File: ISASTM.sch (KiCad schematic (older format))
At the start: 137 parts, among them J1 Bus_ISA_8bit, J2 USB_C_Receptacle_USB2.0, J3 Boot select, J4 USB_C_Receptacle_USB2.0, J5 TagConnect_TC2030_SWD, SW1 Reset, U1 STM32H743IITx, U10 SN74AVC8T245PW, U11 SN74AVC8T245PW, U12 SN74AVC8T245PW, U13 SN74AVC8T245PW, U14 SRV05-4, U15 USB3343, U2 MT48LC16M16A2P, U3 SN74AVC8T245PW, U4 SN74AVC8T245PW, U5 AMS1117-3.3, U6 SN74AVC8T245PW, U7 SN74AVC8T245PW, U8 SN74AVC8T245PW, U9 SN74AVC8T245PW, X1 SG-7050CAN, Y1 26 MHz, Y2 8 MHz

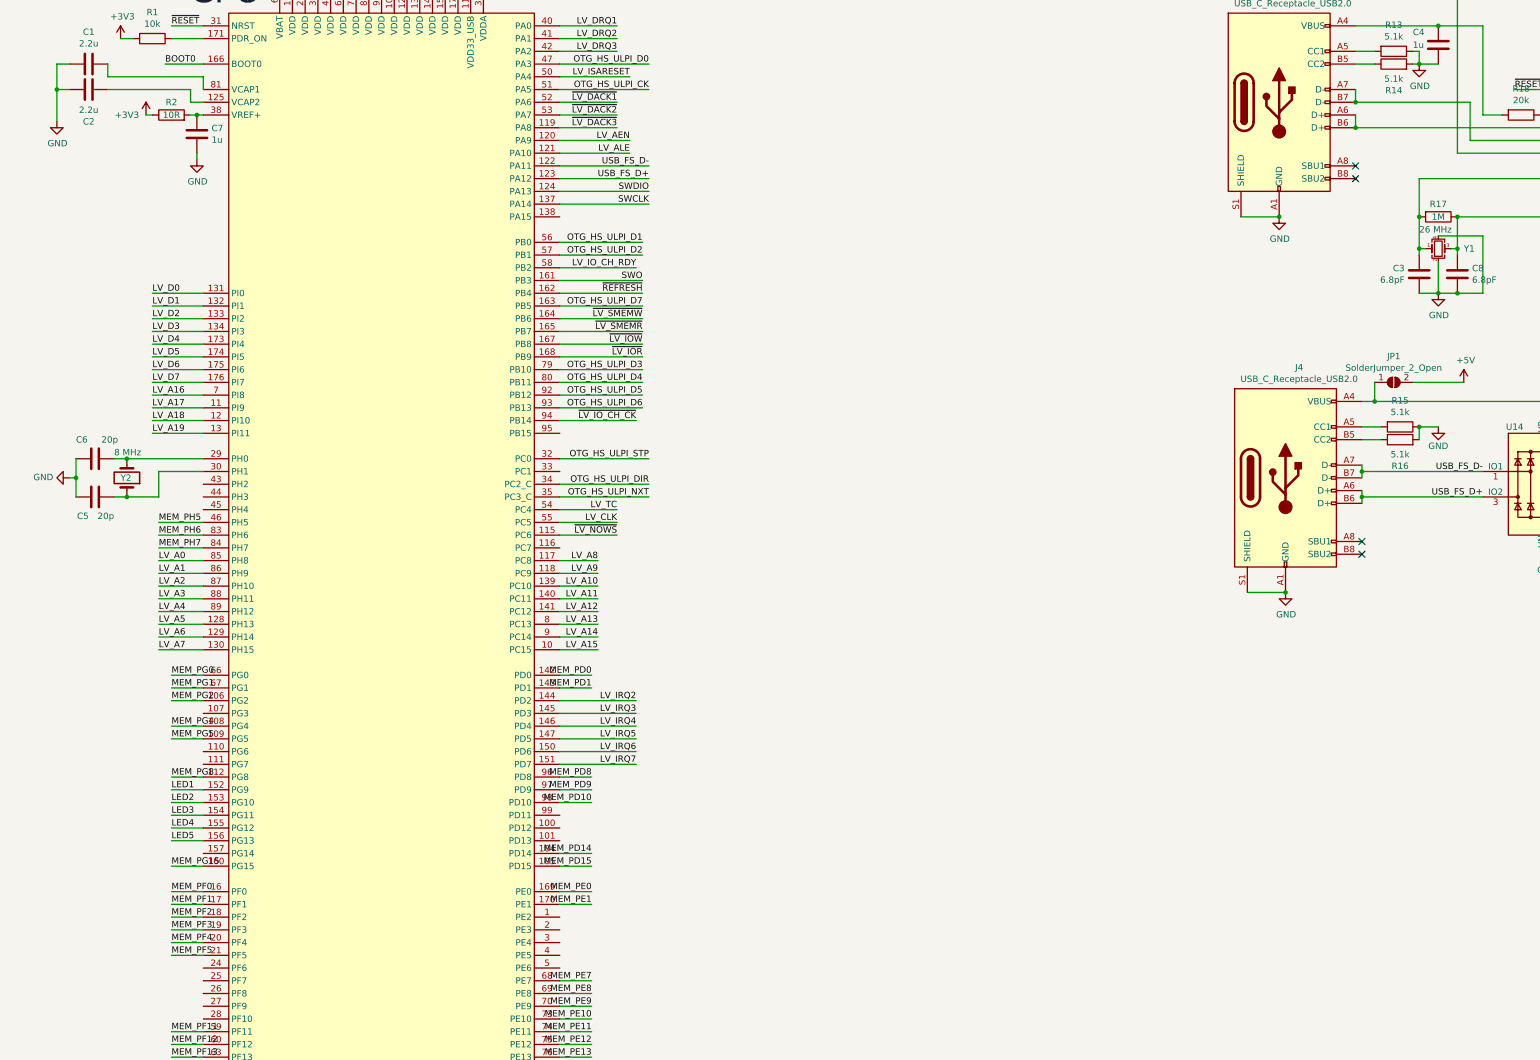
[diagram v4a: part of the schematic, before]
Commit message: Finish fanout and ULPI routing
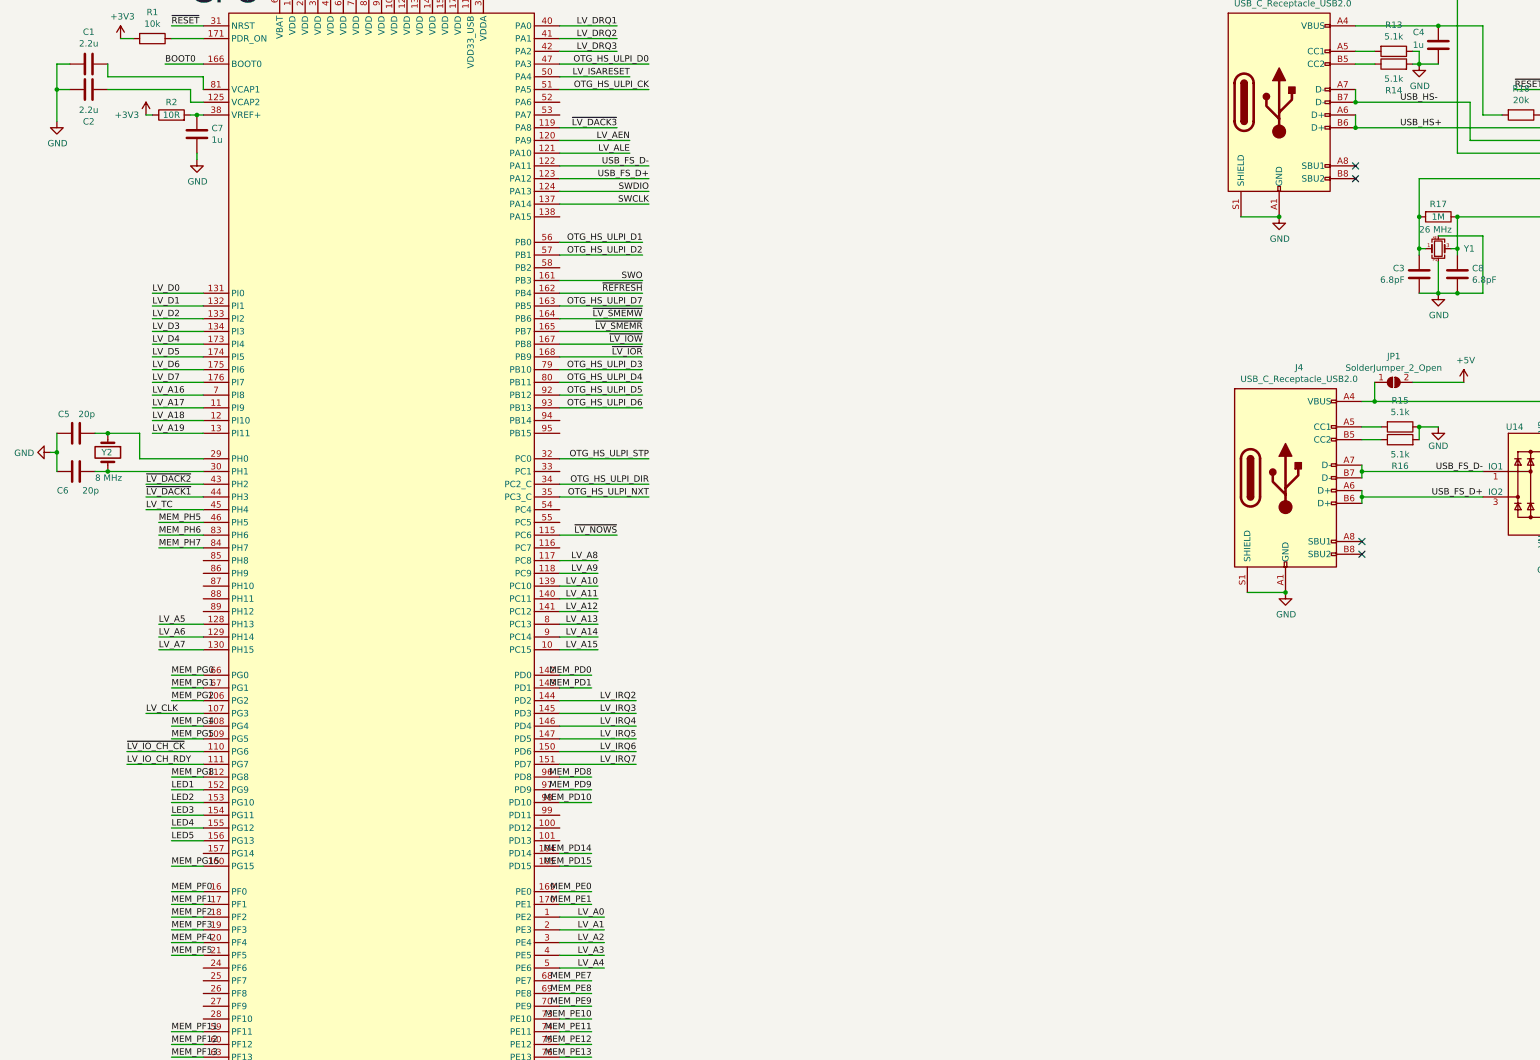
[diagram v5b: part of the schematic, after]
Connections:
- net LV_A0: now also U1.1 (PE2); no longer U1.85 (PH8)
- net LV_A1: now also U1.2 (PE3); no longer U1.86 (PH9)
- net LV_A2: now also U1.3 (PE4); no longer U1.87 (PH10)
- net LV_A3: now also U1.4 (PE5); no longer U1.88 (PH11)
- net LV_A4: now also U1.5 (PE6); no longer U1.89 (PH12)
- net LV_CLK: now also U1.107 (PG3); no longer U1.55 (PC5)
- net LV_IO_CH_RDY: now also U1.111 (PG7); no longer U1.58 (PB2)
- net LV_TC: now also U1.45 (PH4); no longer U1.54 (PC4)
- net ~LV_DACK1: now also U1.44 (PH3); no longer U1.52 (PA6)
- net ~LV_DACK2: now also U1.43 (PH2); no longer U1.53 (PA7)
- net ~LV_IO_CH_CK: now also U1.110 (PG6); no longer U1.94 (PB14)
- net at C6.1, Y2.2: now also U1.30 (PH1); no longer U1.29 (PH0)
- net at C5.2, Y2.1: now also U1.29 (PH0); no longer U1.30 (PH1)
- net USB_HS+: now reaches J2.A6 (D+), J2.B6 (D+), U15.13 (DP)
- net USB_HS-: now reaches J2.A7 (D-), J2.B7 (D-), U15.14 (DM)
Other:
- moved on the sheet: C5, C6, Y2
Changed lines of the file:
@@
 L Device:Crystal Y?
 U 1 1 5FB0B2CB
-P 1450 4750
+P 1300 4550
 AR Path="/5F65970E/5FB0B2CB" Ref="Y?"  Part="1"
 AR Path="/5FB0B2CB" Ref="Y2"  Part="1"
-F 0 "Y2" V 1450 4700 50  0000 L CNN
-F 1 "8 MHz" V 1650 4650 50  0000 L CNN
-F 2 "Crystal:Crystal_SMD_5032-2Pin_5.0x3.2mm" H 1450 4750 50  0001 C CNN
-F 3 "~" H 1450 4750 50  0001 C CNN
-F 4 "C115962" V 1450 4750 50  0001 C CNN "LCSC"
-	1    1450 4750
-	0    1    -1   0
+F 0 "Y2" V 1300 4500 50  0000 L CNN
+F 1 "8 MHz" V 1500 4450 50  0000 L CNN
+F 2 "Crystal:Crystal_SMD_5032-2Pin_5.0x3.2mm" H 1300 4550 50  0001 C CNN
+F 3 "~" H 1300 4550 50  0001 C CNN
+F 4 "C115962" V 1300 4550 50  0001 C CNN "LCSC"
+	1    1300 4550
+	0    1    1    0
 $EndComp
 $Comp
 L Device:C C?
 U 1 1 5FB0B2F2
-P 1200 4900
+P 1050 4400
 AR Path="/5F65970E/5FB0B2F2" Ref="C?"  Part="1"
 AR Path="/5FB0B2F2" Ref="C5"  Part="1"
-F 0 "C5" V 1350 4950 50  0000 L CNN
-F 1 "20p" V 1350 4750 50  0000 L CNN
-F 2 "Capacitor_SMD:C_0402_1005Metric" H 1238 4750 50  0001 C CNN
-F 3 "~" H 1200 4900 50  0001 C CNN
-F 4 "C1554" H 1200 4900 50  0001 C CNN "LCSC"
-	1    1200 4900
-	0    -1   1    0
+F 0 "C5" V 1200 4450 50  0000 L CNN
+F 1 "20p" V 1200 4250 50  0000 L CNN
+F 2 "Capacitor_SMD:C_0402_1005Metric" H 1088 4250 50  0001 C CNN
+F 3 "~" H 1050 4400 50  0001 C CNN
+F 4 "C1554" H 1050 4400 50  0001 C CNN "LCSC"
+	1    1050 4400
+	0    -1   -1   0
 $EndComp
 $Comp
 L Device:C C?
 U 1 1 5FB0B2F9
-P 1200 4600
+P 1050 4700
 AR Path="/5F65970E/5FB0B2F9" Ref="C?"  Part="1"
 AR Path="/5FB0B2F9" Ref="C6"  Part="1"
-F 0 "C6" V 1350 4450 50  0000 L CNN
-F 1 "20p" V 1350 4650 50  0000 L CNN
-F 2 "Capacitor_SMD:C_0402_1005Metric" H 1238 4450 50  0001 C CNN
-F 3 "~" H 1200 4600 50  0001 C CNN
-F 4 "C1554" H 1200 4600 50  0001 C CNN "LCSC"
-	1    1200 4600
-	0    1    -1   0
+F 0 "C6" V 1200 4550 50  0000 L CNN
+F 1 "20p" V 1200 4750 50  0000 L CNN
+F 2 "Capacitor_SMD:C_0402_1005Metric" H 1088 4550 50  0001 C CNN
+F 3 "~" H 1050 4700 50  0001 C CNN
+F 4 "C1554" H 1050 4700 50  0001 C CNN "LCSC"
+	1    1050 4700
+	0    1    1    0
 $EndComp
 Wire Wire Line
-	1050 4900 1050 4750
+	900  4400 900  4550
 $Comp
 L power:GND #PWR?
 U 1 1 5FB0B300
-P 1000 4750
+P 850 4550
 AR Path="/5F65970E/5FB0B300" Ref="#PWR?"  Part="1"
 AR Path="/5FB0B300" Ref="#PWR0123"  Part="1"
-F 0 "#PWR0123" H 1000 4500 50  0001 C CNN
-F 1 "GND" V 1005 4622 50  0000 R CNN
-F 2 "" H 1000 4750 50  0001 C CNN
-F 3 "" H 1000 4750 50  0001 C CNN
-	1    1000 4750
-	0    1    -1   0
+F 0 "#PWR0123" H 850 4300 50  0001 C CNN
+F 1 "GND" V 855 4422 50  0000 R CNN
+F 2 "" H 850 4550 50  0001 C CNN
+F 3 "" H 850 4550 50  0001 C CNN
+	1    850  4550
+	0    1    1    0
 $EndComp
 Wire Wire Line
-	1000 4750 1050 4750
-Connection ~ 1050 4750
+	850  4550 900  4550
+Connection ~ 900  4550
 Wire Wire Line
-	1050 4750 1050 4600
+	900  4550 900  4700
 Wire Wire Line
-	1350 4900 1450 4900
+	1200 4400 1300 4400
 Wire Wire Line
-	1350 4600 1450 4600
+	1200 4700 1300 4700
 $Comp
 L Logic_LevelTranslator:SN74AVC8T245PW U9
@@
 Wire Wire Line
 	3150 13750 3600 13750
-Connection ~ 1450 4600
-Wire Wire Line
-	2050 4700 1700 4700
-Connection ~ 1450 4900
+Connection ~ 1300 4700
 $Comp
 L Interface_USB:USB3343 U15
@@
 	1    0    0    -1
 $EndComp
-Wire Wire Line
-	1700 4700 1700 4900
-Wire Wire Line
-	1450 4900 1700 4900
-Wire Wire Line
-	1450 4600 2050 4600
 Text Label 5550 4600 2    50   ~ 0
 OTG_HS_ULPI_STP
@@
 Text Label 1700 5900 0    50   ~ 0
 LV_A5
-Text Label 1700 5800 0    50   ~ 0
-LV_A4
-Text Label 1700 5700 0    50   ~ 0
-LV_A3
-Text Label 1700 5600 0    50   ~ 0
-LV_A2
-Text Label 1700 5500 0    50   ~ 0
-LV_A1
-Text Label 1700 5400 0    50   ~ 0
-LV_A0
 Wire Wire Line
 	1700 5100 2050 5100
@@
 	1700 5300 2050 5300
 Wire Wire Line
-	1700 5400 2050 5400
-Wire Wire Line
-	1700 5500 2050 5500
-Wire Wire Line
-	1700 5600 2050 5600
-Wire Wire Line
-	1700 5700 2050 5700
-Wire Wire Line
-	1700 5800 2050 5800
-Wire Wire Line
 	1700 5900 2050 5900
 Wire Wire Line
@@
 LV_DRQ1
 Wire Wire Line
-	4850 1800 5300 1800
+	2050 4900 1600 4900
 Wire Wire Line
-	5300 1900 4850 1900
+	1600 4800 2050 4800
 Wire Wire Line
 	4850 2000 5300 2000
-Text Label 5300 1800 2    50   ~ 0
+Text Label 1600 4900 0    50   ~ 0
 ~LV_DACK1
-Text Label 5300 1900 2    50   ~ 0
+Text Label 1600 4800 0    50   ~ 0
 ~LV_DACK2
 Text Label 5300 2000 2    50   ~ 0
 ~LV_DACK3
-Text Label 5300 5000 2    50   ~ 0
-LV_TC
-Wire Wire Line
-	5300 5000 4850 5000
-Text Label 5300 5100 2    50   ~ 0
-LV_CLK
-Wire Wire Line
-	5300 5100 4850 5100
 Text Label 5300 5200 2    50   ~ 0
 ~LV_NOWS
@@
 Text Label 5450 7000 2    50   ~ 0
 LV_IRQ7
-Text Label 5450 4300 2    50   ~ 0
-~LV_IO_CH_CK
-Wire Wire Line
-	5450 3100 4850 3100
 Wire Wire Line
 	5450 6500 4850 6500
@@
 	5450 7000 4850 7000
 Wire Wire Line
-	5450 4300 4850 4300
-Wire Wire Line
 	4850 3500 5500 3500
 Wire Wire Line
@@
 Wire Wire Line
 	4850 3800 5500 3800
-Text Label 5450 3100 2    50   ~ 0
-LV_IO_CH_RDY
 Text Label 1800 7200 0    50   ~ 0
 LED1
@@
 	18400 11900 18450 11900
 Connection ~ 18450 11900
+Text Label 11450 2000 0    50   ~ 0
+USB_HS+
+Text Label 11450 1800 0    50   ~ 0
+USB_HS-
+Wire Wire Line
+	1300 4400 1550 4400
+Wire Wire Line
+	1550 4400 1550 4600
+Wire Wire Line
+	1550 4600 2050 4600
+Connection ~ 1300 4400
+Wire Wire Line
+	1300 4700 2050 4700
+Text Label 1600 5000 0    50   ~ 0
+LV_TC
+Wire Wire Line
+	1600 5000 2050 5000
+Text Label 5200 8500 2    50   ~ 0
+LV_A3
+Text Label 5200 8400 2    50   ~ 0
+LV_A2
+Text Label 5200 8300 2    50   ~ 0
+LV_A1
+Text Label 5200 8200 2    50   ~ 0
+LV_A0
+Wire Wire Line
+	5200 8200 4850 8200
+Wire Wire Line
+	5200 8300 4850 8300
+Wire Wire Line
+	5200 8400 4850 8400
+Wire Wire Line
+	5200 8500 4850 8500
+Text Label 1600 6600 0    50   ~ 0
+LV_CLK
+Wire Wire Line
+	1600 6600 2050 6600
+Text Label 5200 8600 2    50   ~ 0
+LV_A4
+Wire Wire Line
+	5200 8600 4850 8600
+Text Label 1450 6900 0    50   ~ 0
+~LV_IO_CH_CK
+Wire Wire Line
+	1450 6900 2050 6900
+Wire Wire Line
+	1450 7000 2050 7000
+Text Label 1450 7000 0    50   ~ 0
+LV_IO_CH_RDY
 $EndSCHEMATC

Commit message: Partial ISA bus layout
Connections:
- net A16: now also U11.7 (A5); no longer U11.3 (A1)
- net A17: now also U11.8 (A6); no longer U11.4 (A2)
- net A18: now also U11.9 (A7); no longer U11.5 (A3)
- net A19: now also U11.10 (A8); no longer U11.6 (A4)
- net CONTROL1_DIR: now also U1.150 (PD6)
- net CONTROL3_DIR: now also U1.27 (PF9)
- net DATA_DIR: now also U1.146 (PD4)
- net GND: now also U11.18 (B4), U11.19 (B3), U11.20 (B2), U11.21 (B1), U11.3 (A1), U11.4 (A2), U11.5 (A3), U11.6 (A4); no longer U11.10 (A8), U11.14 (B8), U11.15 (B7), U11.16 (B6), U11.17 (B5), U11.7 (A5), U11.8 (A6), U11.9 (A7)
- net LV_A16: now also U11.17 (B5); no longer U11.21 (B1)
- net LV_A17: now also U11.16 (B6); no longer U11.20 (B2)
- net LV_A18: now also U11.15 (B7); no longer U11.19 (B3)
- net LV_A19: now also U11.14 (B8); no longer U11.18 (B4)
- net LV_AEN: now also U1.144 (PD2); no longer U1.120 (PA9)
- net LV_ALE: now also U1.138 (PA15); no longer U1.121 (PA10)
- net LV_CLK: now also U1.41 (PA1); no longer U1.107 (PG3)
- net LV_DRQ1: now also U1.119 (PA8); no longer U1.40 (PA0)
- net LV_DRQ2: now also U1.107 (PG3); no longer U1.41 (PA1)
- net LV_DRQ3: now also U1.115 (PC6); no longer U1.42 (PA2)
- net LV_IRQ2: now also U1.120 (PA9); no longer U1.144 (PD2)
- net LV_IRQ3: now also U1.26 (PF8); no longer U1.145 (PD3)
- net LV_IRQ4: now also U1.25 (PF7); no longer U1.146 (PD4)
- net LV_IRQ5: now also U1.24 (PF6); no longer U1.147 (PD5)
- net LV_IRQ6: now also U1.89 (PH12); no longer U1.150 (PD6)
- net LV_ISARESET: now also U1.157 (PG14); no longer U1.50 (PA4)
- net ~CONTROL1_OE: now also U1.147 (PD5)
- net ~CONTROL3_OE: now also U1.28 (PF10)
- net ~DATA_OE: now also U1.145 (PD3)
- net ~LV_DACK3: now also U1.40 (PA0); no longer U1.119 (PA8)
- net ~LV_NOWS: now also U1.42 (PA2); no longer U1.115 (PC6)
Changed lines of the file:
@@
 Wire Wire Line
 	17450 2800 17950 2800
-Text Label 19150 5050 2    50   ~ 0
+Text Label 19150 5450 2    50   ~ 0
 A19
-Text Label 19150 4950 2    50   ~ 0
+Text Label 19150 5350 2    50   ~ 0
 A18
-Text Label 19150 4850 2    50   ~ 0
+Text Label 19150 5250 2    50   ~ 0
 A17
-Text Label 19150 4750 2    50   ~ 0
+Text Label 19150 5150 2    50   ~ 0
 A16
 Wire Wire Line
-	18950 4750 19150 4750
+	18950 5150 19150 5150
 Wire Wire Line
-	19150 4850 18950 4850
+	19150 5250 18950 5250
 Wire Wire Line
-	18950 4950 19150 4950
+	18950 5350 19150 5350
 Wire Wire Line
-	18950 5050 19150 5050
+	18950 5450 19150 5450
 Text Label 19450 4550 2    50   ~ 0
 ADDRESS_DIR
@@
 Wire Wire Line
 	17650 3300 17950 3300
-Text Label 17650 5050 0    50   ~ 0
+Text Label 17650 5450 0    50   ~ 0
 LV_A19
-Text Label 17650 4950 0    50   ~ 0
+Text Label 17650 5350 0    50   ~ 0
 LV_A18
-Text Label 17650 4850 0    50   ~ 0
+Text Label 17650 5250 0    50   ~ 0
 LV_A17
-Text Label 17650 4750 0    50   ~ 0
+Text Label 17650 5150 0    50   ~ 0
 LV_A16
 Wire Wire Line
-	17650 4750 17950 4750
+	17650 5150 17950 5150
 Wire Wire Line
-	17650 4850 17950 4850
+	17650 5250 17950 5250
 Wire Wire Line
-	17650 4950 17950 4950
+	17650 5350 17950 5350
 Wire Wire Line
-	17650 5050 17950 5050
+	17650 5450 17950 5450
 Connection ~ 18350 4350
 $Comp
@@
 Wire Wire Line
 	16950 3900 16250 3900
-Wire Wire Line
-	17950 5150 17800 5150
-Wire Wire Line
-	17800 5650 18450 5650
-Wire Wire Line
-	17800 5150 17800 5250
 Connection ~ 18450 5650
 Wire Wire Line
-	17800 5250 17950 5250
-Connection ~ 17800 5250
-Wire Wire Line
-	17800 5250 17800 5350
-Wire Wire Line
-	17950 5350 17800 5350
-Connection ~ 17800 5350
-Wire Wire Line
-	17800 5350 17800 5450
-Wire Wire Line
-	17800 5450 17950 5450
-Connection ~ 17800 5450
-Wire Wire Line
-	17800 5450 17800 5650
-Wire Wire Line
-	18450 5650 19100 5650
-Wire Wire Line
-	19100 5150 19100 5250
+	19250 4750 19250 4850
+Connection ~ 19250 4950
 Wire Wire Line
-	18950 5450 19100 5450
-Connection ~ 19100 5450
+	19250 4950 19250 5050
+Connection ~ 19250 4850
 Wire Wire Line
-	19100 5450 19100 5650
-Wire Wire Line
-	18950 5350 19100 5350
-Connection ~ 19100 5350
-Wire Wire Line
-	19100 5350 19100 5450
-Wire Wire Line
-	18950 5250 19100 5250
-Connection ~ 19100 5250
-Wire Wire Line
-	19100 5250 19100 5350
-Wire Wire Line
-	19100 5150 18950 5150
+	19250 4850 19250 4950
 Connection ~ 18350 6150
 $Comp
@@
 Text Label 5500 3800 2    50   ~ 0
 ~LV_IOR
-Text Label 5400 2100 2    50   ~ 0
+Text Label 5400 6500 2    50   ~ 0
 LV_AEN
-Text Label 5400 2200 2    50   ~ 0
-LV_ALE
-Text Label 5400 1600 2    50   ~ 0
-LV_ISARESET
-Wire Wire Line
-	5400 2100 4850 2100
-Wire Wire Line
-	5400 2200 4850 2200
 Wire Wire Line
-	5400 1600 4850 1600
+	5400 6500 4850 6500
 Text Label 5500 3500 2    50   ~ 0
 ~LV_SMEMW
-Text Label 5300 1300 2    50   ~ 0
+Text Label 1600 6600 0    50   ~ 0
 LV_DRQ2
-Text Label 5300 1400 2    50   ~ 0
+Text Label 5300 5200 2    50   ~ 0
 LV_DRQ3
 Wire Wire Line
-	4850 1200 5300 1200
+	4850 2000 5300 2000
 Wire Wire Line
-	5300 1300 4850 1300
+	1600 6600 2050 6600
 Wire Wire Line
-	4850 1400 5300 1400
-Text Label 5300 1200 2    50   ~ 0
+	4850 5200 5300 5200
+Text Label 5300 2000 2    50   ~ 0
 LV_DRQ1
 Wire Wire Line
@@
 	1600 4800 2050 4800
 Wire Wire Line
-	4850 2000 5300 2000
+	4850 1200 5300 1200
 Text Label 1600 4900 0    50   ~ 0
 ~LV_DACK1
 Text Label 1600 4800 0    50   ~ 0
 ~LV_DACK2
-Text Label 5300 2000 2    50   ~ 0
+Text Label 5300 1200 2    50   ~ 0
 ~LV_DACK3
-Text Label 5300 5200 2    50   ~ 0
+Text Label 5300 1400 2    50   ~ 0
 ~LV_NOWS
 Wire Wire Line
-	5300 5200 4850 5200
-Text Label 5450 6500 2    50   ~ 0
+	5300 1400 4850 1400
+Text Label 5450 2100 2    50   ~ 0
 LV_IRQ2
-Text Label 5450 6600 2    50   ~ 0
-LV_IRQ3
-Text Label 5450 6700 2    50   ~ 0
+Text Label 1450 8700 0    50   ~ 0
 LV_IRQ4
-Text Label 5450 6800 2    50   ~ 0
+Text Label 1450 8600 0    50   ~ 0
 LV_IRQ5
-Text Label 5450 6900 2    50   ~ 0
+Text Label 1450 5800 0    50   ~ 0
 LV_IRQ6
 Text Label 5450 7000 2    50   ~ 0
 LV_IRQ7
 Wire Wire Line
-	5450 6500 4850 6500
-Wire Wire Line
-	5450 6600 4850 6600
+	5450 2100 4850 2100
 Wire Wire Line
-	5450 6700 4850 6700
+	1450 8700 2050 8700
 Wire Wire Line
-	5450 6800 4850 6800
+	1450 8600 2050 8600
 Wire Wire Line
-	5450 6900 4850 6900
+	1450 5800 2050 5800
 Wire Wire Line
 	5450 7000 4850 7000
@@
 Wire Wire Line
 	5200 8500 4850 8500
-Text Label 1600 6600 0    50   ~ 0
+Text Label 5300 1300 2    50   ~ 0
 LV_CLK
 Wire Wire Line
-	1600 6600 2050 6600
+	5300 1300 4850 1300
 Text Label 5200 8600 2    50   ~ 0
 LV_A4
@@
 Text Label 1450 7000 0    50   ~ 0
 LV_IO_CH_RDY
+Text Label 1500 7700 0    50   ~ 0
+LV_ISARESET
+Wire Wire Line
+	1500 7700 2050 7700
+Text Label 5400 2700 2    50   ~ 0
+LV_ALE
+Wire Wire Line
+	5400 2700 4850 2700
+Text Label 1450 8800 0    50   ~ 0
+LV_IRQ3
+Wire Wire Line
+	1450 8800 2050 8800
+Wire Wire Line
+	4850 6600 5400 6600
+Text Label 5400 6600 2    50   ~ 0
+~DATA_OE
+Wire Wire Line
+	4850 6700 5400 6700
+Text Label 5400 6700 2    50   ~ 0
+DATA_DIR
+Wire Wire Line
+	4850 6800 5400 6800
+Text Label 5400 6800 2    50   ~ 0
+~CONTROL1_OE
+Wire Wire Line
+	4850 6900 5400 6900
+Text Label 5400 6900 2    50   ~ 0
+CONTROL1_DIR
+Wire Wire Line
+	18950 4750 19250 4750
+Wire Wire Line
+	18950 4850 19250 4850
+Wire Wire Line
+	18950 4950 19250 4950
+Wire Wire Line
+	18950 5050 19250 5050
+Wire Wire Line
+	18450 5650 19250 5650
+Wire Wire Line
+	19250 5650 19250 5050
+Connection ~ 19250 5050
+Wire Wire Line
+	17550 4750 17550 4850
+Connection ~ 17550 4950
+Wire Wire Line
+	17550 4950 17550 5050
+Connection ~ 17550 4850
+Wire Wire Line
+	17550 4850 17550 4950
+Wire Wire Line
+	17550 5650 17550 5050
+Connection ~ 17550 5050
+Wire Wire Line
+	17550 4750 17950 4750
+Wire Wire Line
+	17550 4850 17950 4850
+Wire Wire Line
+	17550 4950 17950 4950
+Wire Wire Line
+	17550 5050 17950 5050
+Wire Wire Line
+	17550 5650 18450 5650
+Text Label 1450 9000 0    50   ~ 0
+~CONTROL3_OE
+Wire Wire Line
+	1450 9000 2050 9000
+Text Label 1450 8900 0    50   ~ 0
+CONTROL3_DIR
+Wire Wire Line
+	2050 8900 1450 8900
 $EndSCHEMATC
